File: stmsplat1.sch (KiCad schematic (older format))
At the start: 23 parts, among them CN1 10n, CN10 Conn_01x34_Male, CN7 Conn_01x20_Male, CN8 Conn_01x16_Male, CN9 Conn_01x30_Male, J3 Conn_Coaxial, U1 NUCLEO144-F746ZG, U2 AD8310, U3 MCP6S93-X_UN, U4 ublox_chinese_PCB_module, U5 Opamp_Quad_MCP6024

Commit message: Added more
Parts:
- added C10, C11, C5, C6, C7, C9: 47n, Capacitor_SMD:C_1210_3225Metric_Pad1.42x2.65mm_HandSolder, symbol Device:C_Small
- added C12, C14: 1uF, Capacitor_THT:CP_Radial_D5.0mm_P2.50mm, symbol Device:CP
- added C13: 10uF, Capacitor_THT:CP_Radial_D5.0mm_P2.50mm, symbol Device:CP
- added C15: 100nF, Capacitor_THT:C_Disc_D7.5mm_W2.5mm_P5.00mm, symbol Device:C_Small
- added C16, C17: 100uF, Capacitor_THT:CP_Radial_D5.0mm_P2.50mm, symbol Device:CP
- added C8: 25pF, Capacitor_THT:C_Disc_D7.5mm_W2.5mm_P5.00mm, symbol Device:C_Small
- added D2, D3, D4, D5, D6, D7: LED, LED_SMD:LED_PLCC-2, symbol Device:LED
- added J2: Conn_01x04_Male, Connector_PinHeader_2.54mm:PinHeader_1x04_P2.54mm_Vertical, symbol Connector:Conn_01x04_Male
- added R3: 53R, Capacitor_SMD:C_1210_3225Metric_Pad1.42x2.65mm_HandSolder, symbol Device:R_Small
- added RN2, RN3: 470R, Resistor_SMD:R_Array_Convex_4x1206, symbol Device:R_Pack04
- added TP10, TP11, TP12, TP13, TP3, TP4, TP5, TP6, TP7, TP8, TP9: TestPoint, TestPoint:TestPoint_Loop_D1.80mm_Drill1.0mm_Beaded, symbol Connector:TestPoint
- added U10: MPL315A2, Package_LGA:LGA-8_3x5mm_P1.25mm, symbol splatlib:MPL315A2
- added U3, U9: HMC544A-RF_Switch, Package_TO_SOT_SMD:SOT-23-6_Handsoldering, symbol splatsyms:HMC544A-RF_Switch
- added U7: ADG729, Package_SO:TSSOP-16_4.4x5mm_P0.65mm, symbol Analog_Switch:ADG729
- added U8: 74HC04, symbol 74xx:74HC04
- C4: renamed from C1; value 1uF -> 10uF
- renumbered C2 to C1, C3 to C2, C4 to C3, CN8 to CN1, CN9 to CN2, CN7 to CN3, CN10 to CN4, CN1 to CN5, J3 to J1, R2 to R1, R1 to R2, RN3 to RN1, U4 to U2, U5 to U4, U2 to U5, U3 to U6
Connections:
- net labels added: 5V0, AMPOUT, DAC1, HALF3V3, LOGOUT, NXRX, NXTX
- wire segments 88 -> 231
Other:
- moved on the sheet: C2, C3, D1, J1, L1, L2, R1, R2, RN1, U4A, U4B, U4C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

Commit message: Zigbee added
Trial placement 1
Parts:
- added U11: XBee_SMT, RF_Module:Digi_XBee_SMT, symbol RF_ZigBee:XBee_SMT
- U10: symbol splatlib:MPL315A2 -> stmsplat1-rescue:MPL315A2-splatlib
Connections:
- wire segments 231 -> 232
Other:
- moved on the sheet: C1, C15, CN5, D2, D3, D4, D5, D6, D7, RN2, RN3, TP11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

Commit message: XBee changes, more STM interconnect detail
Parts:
- removed U11: XBee_SMT, RF_Module:Digi_XBee_SMT, symbol RF_ZigBee:XBee_SMT
- added C18: 10uF, Capacitor_THT:CP_Radial_D5.0mm_P2.50mm, symbol Device:CP
- added D8: LED, LED_SMD:LED_PLCC-2, symbol Device:LED
- added TP1, TP2: TestPoint, TestPoint:TestPoint_Loop_D1.80mm_Drill1.0mm_Beaded, symbol Connector:TestPoint
- added U11: XBee3, spatboard:XBEE-22MM-TH, symbol splatlib:XBee3
- renumbered D4 to D1, D3 to D2, D5 to D3, D2 to D4, D7 to D5, D1 to D7
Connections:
- net labels added: NXT_RX, NXT_TX, UART4, XB_PIO4
- net labels removed: NXRX, NXTX
- wire segments 232 -> 277
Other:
- moved on the sheet: TP11, TP12, TP13

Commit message: Initial design captured
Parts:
- removed CN5: 10n, spatboard:C_Array_Convex_4x1206, symbol stmsplat1-rescue:C_Pack04-c_pack04-splatsyms
- added C19: 1uF, Capacitor_THT:CP_Radial_D5.0mm_P2.50mm, symbol Device:CP
- added C20: 470pF, Capacitor_SMD:C_0805_2012Metric_Pad1.15x1.40mm_HandSolder, symbol Device:C
- added LS1: Speaker, Buzzer_Beeper:MagneticBuzzer_Kingstate_KCG0601, symbol Device:Speaker
- added RN4: 4K7, Resistor_SMD:R_Array_Convex_4x1206, symbol Device:R_Pack04
- added U12: MIC5219-3.3YM5, Package_TO_SOT_SMD:SOT-23-5, symbol Regulator_Linear:MIC5219-3.3YM5
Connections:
- net +3V3: now also U12.3 (EN); no longer C1.1, C12.1, C13.1, C16.1, C18.1, FB1.1, RN3.5 (R4.2), U10.1 (VDD), U10.4 (VDDIO), U11.1 (VCC), U2.1 (VCC), U8.14 (VCC)
- net +5V: now also U12.1 (IN)
- net DAC1: now also U7.10 (S4B); no longer TP9.1
- net GND: now also C20.2, LS1.2, U12.2 (GND)
- net LOGOUT: now also U7.12 (S2B)
- net PA3: now also U4.3 (+), U7.8 (DA)
- net PB10: now also U2.5 (TIMEPULSE), RN4.1 (R1.1)
- net PC2: now also U6.8 (SO)
- net PC3: now also U6.7 (SI)
- net PD13: now also RN2.5 (R4.2); no longer RN2.6 (R3.2)
- net PD14: now also RN2.6 (R3.2); no longer RN2.5 (R4.2)
- net PD3: now also U6.9 (SCK)
- net PE10: now also U11.9 (SLEEPRQ/DIO8/~DTR)
- net PG2: now also U6.6 (*CS)
- net at U4.5 (+): now also U4.12 (+), U7.9 (DB)
- net at U4.6 (-): now also TP9.1, U4.7
- net at U4.13 (-): now also U4.14, C19.1
- net at U4.1: now also TP3.1, U4.2 (-)
- net at C10.2, L1.2, R1.1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: no longer TP7.1
- net SPEAKER_TIM4CH3: now reaches U7.11 (S3B)
- net at C9.2, U3.1 (RF2): no longer TP3.1
- net at U8.5: now also RN4.3 (R3.1)
- net at U11.7 (PWM1/DIO11): now also U8.9
- net at U8.8: now also TP7.1
- net at U8.11: now also RN4.2 (R2.1)
- net at U8.13: now also RN4.4 (R4.1)
- new net: C19.2, LS1.1
- new net: C20.1, U12.4 (BP)
- new net P3V3: C1.1, C12.1, C13.1, C16.1, C18.1, FB1.1, RN3.5 (R4.2), RN4.5 (R4.2), RN4.6 (R3.2), RN4.7 (R2.2), RN4.8 (R1.2), U10.1 (VDD), U10.4 (VDDIO), U11.1 (VCC), U12.5 (OUT), U2.1 (VCC), U8.14 (VCC)
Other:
- moved on the sheet: D8, FB2, J2, TP2, TP9, U4A, U4B, U4D, U8C, U8D, U8E, U8F

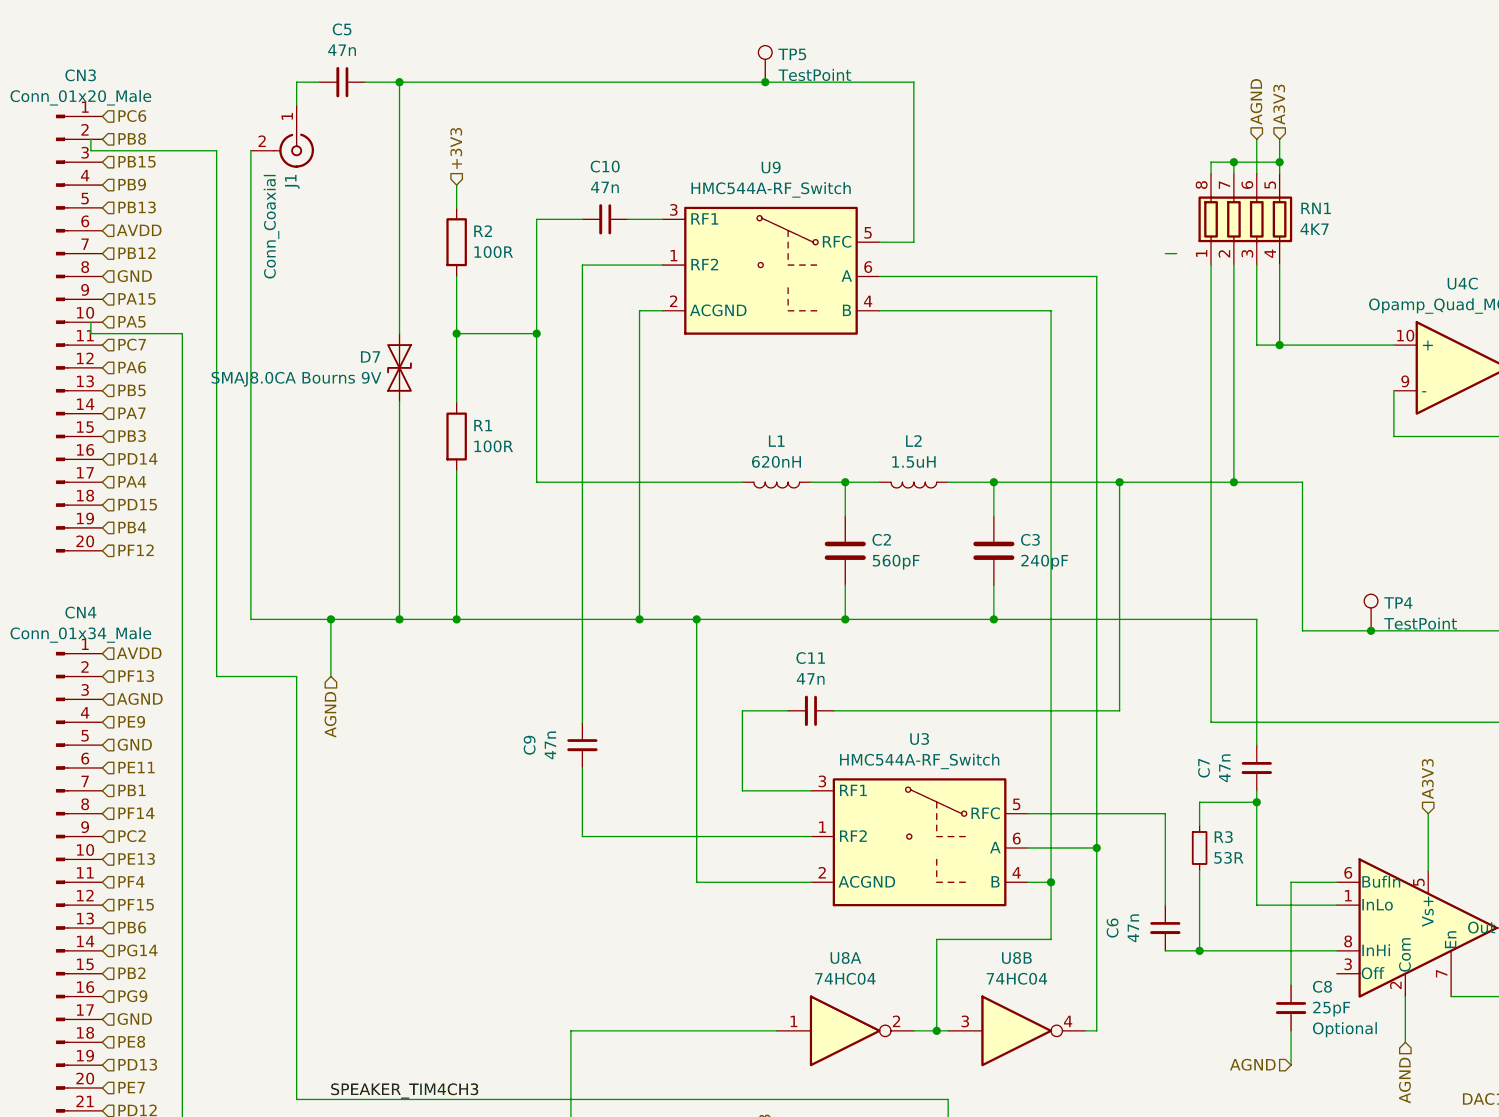
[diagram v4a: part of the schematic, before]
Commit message: Chenged input and filter matching arrangement
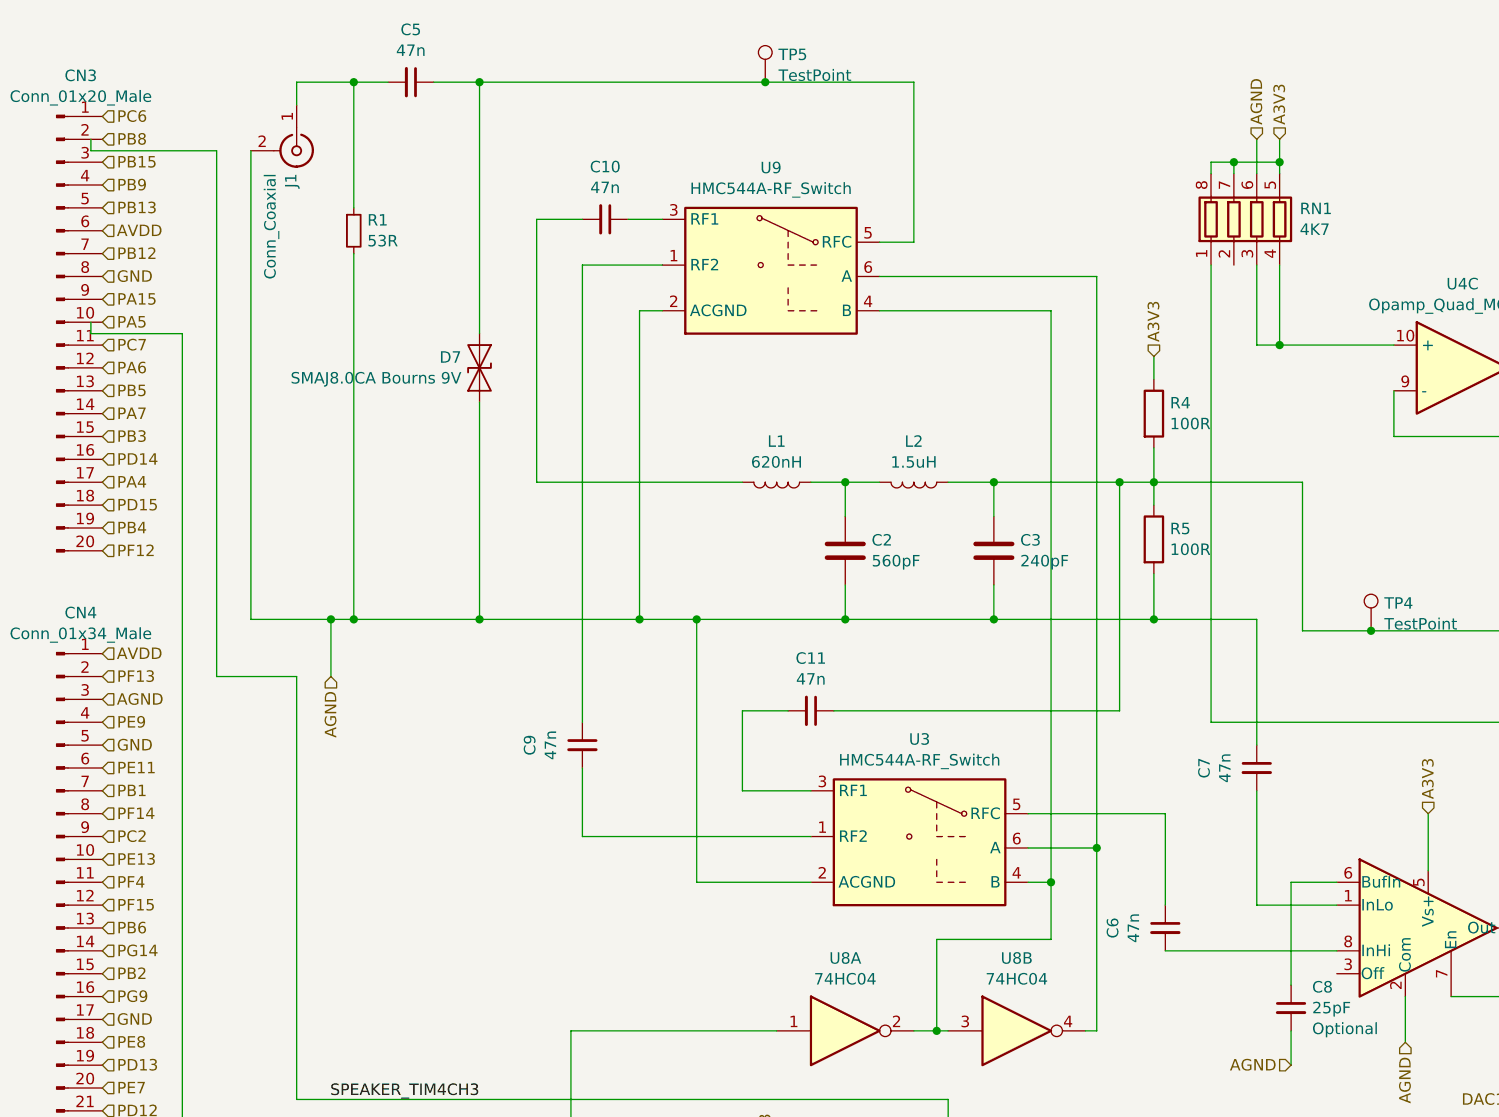
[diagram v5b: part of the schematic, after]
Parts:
- removed R1, R2: 100R, Resistor_SMD:R_2010_5025Metric_Pad1.52x2.65mm_HandSolder, symbol Device:R
- removed R3: 53R, Capacitor_SMD:C_1210_3225Metric_Pad1.42x2.65mm_HandSolder, symbol Device:R_Small
- added R1: 53R, Capacitor_SMD:C_1210_3225Metric_Pad1.42x2.65mm_HandSolder, symbol Device:R_Small
- added R4, R5: 100R, Resistor_SMD:R_2010_5025Metric_Pad1.52x2.65mm_HandSolder, symbol Device:R
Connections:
- net A3V3: now also R4.1
- net AGND: now also R1.2, R5.2
- net at C5.2, J1.1 (In): now also R1.1
- net at C11.1, C3.1, L2.1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: now also R4.2, R5.1; no longer RN1.2 (R2.1)
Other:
- moved on the sheet: C5, D7
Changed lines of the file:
@@
 AGND
-$Comp
-L Device:R R1
-U 1 1 5BE50750
-P 6850 2500
-F 0 "R1" H 6920 2546 50  0000 L CNN
-F 1 "100R" H 6920 2455 50  0000 L CNN
-F 2 "Resistor_SMD:R_2010_5025Metric_Pad1.52x2.65mm_HandSolder" V 6780 2500 50  0001 C CNN
-F 3 "~" H 6850 2500 50  0001 C CNN
-	1    6850 2500
-	1    0    0    -1
-$EndComp
-$Comp
-L Device:R R2
-U 1 1 5BE50836
-P 6850 1650
-F 0 "R2" H 6920 1696 50  0000 L CNN
-F 1 "100R" H 6920 1605 50  0000 L CNN
-F 2 "Resistor_SMD:R_2010_5025Metric_Pad1.52x2.65mm_HandSolder" V 6780 1650 50  0001 C CNN
-F 3 "~" H 6850 1650 50  0001 C CNN
-	1    6850 1650
-	1    0    0    -1
-$EndComp
-Text HLabel 6850 1400 1    50   Input ~ 0
-+3V3
 $Comp
 L Device:D_TVS D7
 U 1 1 5BE6C923
-P 6600 2200
-F 0 "D7" V 6554 2279 50  0000 L CNN
-F 1 "SMAJ8.0CA Bourns 9V" V 6645 2279 50  0000 L CNN
-F 2 "Diode_SMD:D_SMA_Handsoldering" H 6600 2200 50  0001 C CNN
-F 3 "http://www.farnell.com/datasheets/2076055.pdf?_ga=2.113895617.736118577.1541708831-952325772.1540441496" H 6600 2200 50  0001 C CNN
-	1    6600 2200
+P 6950 2200
+F 0 "D7" V 6904 2279 50  0000 L CNN
+F 1 "SMAJ8.0CA Bourns 9V" V 6995 2279 50  0000 L CNN
+F 2 "Diode_SMD:D_SMA_Handsoldering" H 6950 2200 50  0001 C CNN
+F 3 "http://www.farnell.com/datasheets/2076055.pdf?_ga=2.113895617.736118577.1541708831-952325772.1540441496" H 6950 2200 50  0001 C CNN
+	1    6950 2200
 	0    -1   1    0
 $EndComp
-Wire Wire Line
-	6850 1400 6850 1500
-Wire Wire Line
-	10250 2700 10250 1750
 Wire Wire Line
 	10450 1300 10250 1300
@@
 	1    0    0    -1
 $EndComp
-Wire Wire Line
-	6150 950  6250 950
 $Comp
 L Device:C_Small C5
 U 1 1 5BF5E583
-P 6350 950
-F 0 "C5" V 6121 950 50  0000 C CNN
-F 1 "47n" V 6212 950 50  0000 C CNN
-F 2 "Capacitor_SMD:C_1210_3225Metric_Pad1.42x2.65mm_HandSolder" H 6350 950 50  0001 C CNN
-F 3 "~" H 6350 950 50  0001 C CNN
-	1    6350 950
+P 6650 950
+F 0 "C5" V 6421 950 50  0000 C CNN
+F 1 "47n" V 6512 950 50  0000 C CNN
+F 2 "Capacitor_SMD:C_1210_3225Metric_Pad1.42x2.65mm_HandSolder" H 6650 950 50  0001 C CNN
+F 3 "~" H 6650 950 50  0001 C CNN
+	1    6650 950
 	0    1    1    0
 $EndComp
@@
 $EndComp
 Wire Wire Line
-	9200 3300 10350 3300
+	9200 3300 9900 3300
 Wire Wire Line
 	10350 3300 10350 3850
@@
 $EndComp
 Wire Wire Line
-	9950 4750 10100 4750
-Wire Wire Line
 	9350 4150 9950 4150
 Wire Wire Line
@@
 Wire Wire Line
 	8100 4050 8400 4050
-Connection ~ 9750 2700
-Wire Wire Line
-	9750 2700 10250 2700
-Wire Wire Line
-	6600 2350 6600 3300
-Connection ~ 6600 3300
+Wire Wire Line
+	6950 2350 6950 3300
+Connection ~ 6950 3300
 $Comp
 L Device:C_Small C8
@@
 	8850 1650 8700 1650
 Wire Wire Line
-	6450 950  6600 950
+	6750 950  6950 950
 Wire Wire Line
 	7200 2700 8100 2700
-Connection ~ 6600 950
-Wire Wire Line
-	6600 3300 6850 3300
+Connection ~ 6950 950
 Wire Wire Line
 	7750 1750 7400 1750
 Wire Wire Line
-	6850 1800 6850 2050
-Wire Wire Line
-	6600 950  6600 2050
-Wire Wire Line
-	6850 2650 6850 3300
-Connection ~ 6850 3300
-Wire Wire Line
-	6850 2050 7200 2050
-Connection ~ 6850 2050
-Wire Wire Line
-	6850 2050 6850 2350
-Connection ~ 7200 2050
-Wire Wire Line
-	7200 2050 7200 2700
-$Comp
-L Device:R_Small R3
-U 1 1 5BFA781B
-P 10100 4300
-F 0 "R3" H 10159 4346 50  0000 L CNN
-F 1 "53R" H 10159 4255 50  0000 L CNN
-F 2 "Capacitor_SMD:C_1210_3225Metric_Pad1.42x2.65mm_HandSolder" H 10100 4300 50  0001 C CNN
-F 3 "~" H 10100 4300 50  0001 C CNN
-	1    10100 4300
-	1    0    0    -1
-$EndComp
-Wire Wire Line
-	10100 4200 10100 4100
-Wire Wire Line
-	10100 4100 10350 4100
-Wire Wire Line
-	10350 4050 10350 4100
-Connection ~ 10350 4100
-Wire Wire Line
-	10350 4100 10350 4550
+	6950 950  6950 2050
 Wire Wire Line
 	8550 3300 9200 3300
 Connection ~ 6300 3300
 Wire Wire Line
-	6300 3300 6600 3300
+	6300 3300 6400 3300
 Connection ~ 10450 2100
 Wire Wire Line
@@
 Wire Wire Line
 	9950 4150 9950 4550
-Wire Wire Line
-	10100 4400 10100 4750
-Connection ~ 10100 4750
-Wire Wire Line
-	10100 4750 10700 4750
 Wire Wire Line
 	7750 1950 7650 1950
@@
 Wire Wire Line
 	10550 3350 10550 2700
-Wire Wire Line
-	10550 2700 10250 2700
-Connection ~ 10250 2700
 Connection ~ 12650 5100
 Wire Wire Line
@@
 	8950 5100 9000 5100
 Wire Wire Line
-	9950 1700 10000 1700
-Wire Wire Line
-	6600 950  8200 950
-Wire Wire Line
-	6850 3300 7650 3300
+	6950 950  8200 950
 Connection ~ 8200 950
 Wire Wire Line
@@
 Wire Wire Line
 	7400 1550 7200 1550
-Wire Wire Line
-	7200 1550 7200 2050
 $Comp
 L Device:C_Small C11
@@
 	12000 5700 13150 5700
 Connection ~ 12000 5200
+$Comp
+L Device:R R5
+U 1 1 5BF77C69
+P 9900 2950
+F 0 "R5" H 9970 2996 50  0000 L CNN
+F 1 "100R" H 9970 2905 50  0000 L CNN
+F 2 "Resistor_SMD:R_2010_5025Metric_Pad1.52x2.65mm_HandSolder" V 9830 2950 50  0001 C CNN
+F 3 "~" H 9900 2950 50  0001 C CNN
+	1    9900 2950
+	1    0    0    -1
+$EndComp
+$Comp
+L Device:R R4
+U 1 1 5BF77C6F
+P 9900 2400
+F 0 "R4" H 9970 2446 50  0000 L CNN
+F 1 "100R" H 9970 2355 50  0000 L CNN
+F 2 "Resistor_SMD:R_2010_5025Metric_Pad1.52x2.65mm_HandSolder" V 9830 2400 50  0001 C CNN
+F 3 "~" H 9900 2400 50  0001 C CNN
+	1    9900 2400
+	1    0    0    -1
+$EndComp
+Wire Wire Line
+	9900 3100 9900 3300
+Wire Wire Line
+	9900 2550 9900 2700
+Text HLabel 9900 2150 1    50   Input ~ 0
+A3V3
+Wire Wire Line
+	9900 2150 9900 2250
+Connection ~ 9900 3300
+Wire Wire Line
+	9900 3300 10350 3300
+Wire Wire Line
+	9750 2700 9900 2700
+Connection ~ 9750 2700
+Connection ~ 9900 2700
+Wire Wire Line
+	9900 2700 9900 2800
+Wire Wire Line
+	9900 2700 10550 2700
+Wire Wire Line
+	7200 1550 7200 2700
+Wire Wire Line
+	6950 3300 7650 3300
+$Comp
+L Device:R_Small R1
+U 1 1 5C0A226D
+P 6400 1600
+F 0 "R1" H 6459 1646 50  0000 L CNN
+F 1 "53R" H 6459 1555 50  0000 L CNN
+F 2 "Capacitor_SMD:C_1210_3225Metric_Pad1.42x2.65mm_HandSolder" H 6400 1600 50  0001 C CNN
+F 3 "~" H 6400 1600 50  0001 C CNN
+	1    6400 1600
+	1    0    0    -1
+$EndComp
+Wire Wire Line
+	10350 4050 10350 4550
+Wire Wire Line
+	9950 4750 10700 4750
+Wire Wire Line
+	6150 950  6400 950
+Wire Wire Line
+	6400 950  6400 1500
+Connection ~ 6400 950
+Wire Wire Line
+	6400 950  6550 950
+Wire Wire Line
+	6400 1700 6400 3300
+Connection ~ 6400 3300
+Wire Wire Line
+	6400 3300 6950 3300
 $EndSCHEMATC

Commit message: Stuff done by paul
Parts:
- U11: symbol splatlib:XBee3 -> stmsplat1-rescue:XBee3-splatlib
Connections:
- wire segments 383 -> 380
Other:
- moved on the sheet: CN3, D7, U1
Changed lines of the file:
@@
 L MCU_Module:NUCLEO144-F746ZG U1
 U 1 1 5BCFF0C9
-P 3350 4550
-F 0 "U1" H 3350 8436 50  0000 C CNN
-F 1 "NUCLEO144-F746ZG" H 3350 8527 50  0000 C CNN
-F 2 "spatboard:ST_Nucleo_144_Large_Daughter" H 4200 900 50  0001 L CNN
-F 3 "" H 2450 4850 50  0001 C CNN
-	1    3350 4550
+P 3750 5400
+F 0 "U1" H 3750 9286 50  0000 C CNN
+F 1 "NUCLEO144-F746ZG" H 3750 9377 50  0000 C CNN
+F 2 "spatboard:ST_Nucleo_144_Large_Daughter" H 4600 1750 50  0001 L CNN
+F 3 "" H 2850 5700 50  0001 C CNN
+	1    3750 5400
 	-1   0    0    1
 $EndComp
@@
 L Connector:Conn_01x20_Male CN3
 U 1 1 5BD04C2E
-P 5100 2000
-F 0 "CN3" H 5206 3078 50  0000 C CNN
-F 1 "Conn_01x20_Male" H 5206 2987 50  0000 C CNN
-F 2 "spatboard:IDC-Pins_2x10_P2.54mm_Vertical" H 5100 2000 50  0001 C CNN
-F 3 "" H 5100 2000 50  0001 C CNN
-	1    5100 2000
+P 5500 2850
+F 0 "CN3" H 5606 3928 50  0000 C CNN
+F 1 "Conn_01x20_Male" H 5606 3837 50  0000 C CNN
+F 2 "spatboard:IDC-Pins_2x10_P2.54mm_Vertical" H 5500 2850 50  0001 C CNN
+F 3 "" H 5500 2850 50  0001 C CNN
+	1    5500 2850
 	1    0    0    -1
 $EndComp
@@
 Text HLabel 5300 2200 2    50   Input ~ 0
 PA6
-Text HLabel 5300 2300 2    50   Input ~ 0
+Text HLabel 5700 3150 2    50   Input ~ 0
 PB5
 Text HLabel 5300 2400 2    50   Input ~ 0
@@
 L Device:D_TVS D7
 U 1 1 5BE6C923
-P 6950 2200
-F 0 "D7" V 6904 2279 50  0000 L CNN
-F 1 "SMAJ8.0CA Bourns 9V" V 6995 2279 50  0000 L CNN
-F 2 "Diode_SMD:D_SMA_Handsoldering" H 6950 2200 50  0001 C CNN
-F 3 "http://www.farnell.com/datasheets/2076055.pdf?_ga=2.113895617.736118577.1541708831-952325772.1540441496" H 6950 2200 50  0001 C CNN
-	1    6950 2200
+P 7350 3050
+F 0 "D7" V 7304 3129 50  0000 L CNN
+F 1 "SMAJ8.0CA Bourns 9V" V 7395 3129 50  0000 L CNN
+F 2 "Diode_SMD:D_SMA_Handsoldering" H 7350 3050 50  0001 C CNN
+F 3 "http://www.farnell.com/datasheets/2076055.pdf?_ga=2.113895617.736118577.1541708831-952325772.1540441496" H 7350 3050 50  0001 C CNN
+	1    7350 3050
 	0    -1   1    0
 $EndComp
@@
 $EndComp
 Wire Wire Line
-	5950 1250 5950 3300
+	6350 2100 6350 4150
 Wire Wire Line
 	6150 1050 6150 950
@@
 	8100 4050 8400 4050
 Wire Wire Line
-	6950 2350 6950 3300
-Connection ~ 6950 3300
+	7350 3200 7350 4150
 $Comp
 L Device:C_Small C8
@@
 	8550 3300 9200 3300
 Connection ~ 6300 3300
-Wire Wire Line
-	6300 3300 6400 3300
 Connection ~ 10450 2100
 Wire Wire Line
@@
 	7750 1950 7650 1950
 Wire Wire Line
-	7650 1950 7650 3300
-Connection ~ 7650 3300
-Wire Wire Line
-	7650 3300 7900 3300
+	8050 2800 8050 4150
 Wire Wire Line
 	8400 4450 7900 4450
@@
 $EndComp
 Wire Wire Line
-	7400 1750 7400 3750
+	7800 2600 7800 4600
 Wire Wire Line
 	7400 3950 7400 4250
@@
 	8350 8100 8350 8000
 $Comp
-L splatlib:XBee3 U11
+L stmsplat1-rescue:XBee3-splatlib U11
 U 1 1 5BFA172B
 P 7350 7600
@@
 	8200 6300 5650 6300
 Wire Wire Line
-	5650 2050 5650 6300
-Connection ~ 5650 6300
+	6050 2900 6050 7150
 Wire Wire Line
 	5650 6300 5650 6600
@@
 	5250 1250 5800 1250
 Wire Wire Line
-	5800 1250 5800 3550
+	6200 2100 6200 4400
 Wire Wire Line
 	5800 3550 6150 3550
@@
 	9900 2700 10550 2700
 Wire Wire Line
-	7200 1550 7200 2700
-Wire Wire Line
-	6950 3300 7650 3300
+	7600 2400 7600 3550
 $Comp
 L Device:R_Small R1
@@
 	6400 950  6550 950
 Wire Wire Line
-	6400 1700 6400 3300
-Connection ~ 6400 3300
-Wire Wire Line
-	6400 3300 6950 3300
+	6800 2550 6800 4150
+Wire Wire Line
+	6300 3300 7900 3300
 $EndSCHEMATC
